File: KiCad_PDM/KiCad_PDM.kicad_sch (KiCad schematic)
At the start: 0 parts

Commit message: initial commit
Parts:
- added C1, C2: 1uF, symbol Device:C
- added C3: 2.2nF, symbol Device:C
- added C4: 10nF, symbol Device:C
- added D1, D4: MMSZ47202T1G, Diode_SMD:D_SOD-123, symbol PDM:onsemi MMSZ4702T1G
- added D2, D3: FR107, Diode_SMD:D_SOD-123, symbol PDM:JSMSEMI FR107
- added J1: 6437288-1, 6437288-1, symbol 6437288-1:6437288-1
- added R1: 39K, symbol Device:R
- added R2: 1K, symbol Device:R
- added R3: 5.1K, symbol Device:R
- added R4: 50, symbol Device:R
- added U1: NSG2000, Package_SO:SOP-8_3.76x4.96mm_P1.27mm, symbol PDM:NSG2000
- added U2: 2N7002, Package_TO_SOT_SMD:SOT-23_Handsoldering, symbol PDM:Nexperia 2N7002BK,215
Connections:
- new net: D4.1, R3.2, R4.1
- new net: C4.1, R4.2
- new net: C3.1, R1.2, R2.1, U1.3 (Osc)
- new net: R2.2, U2.3
- new net: C2.1, D1.1, D2.1, U1.8 (BST)
- new net: C2.2, D1.2, D3.2, U1.6 (TS)
- new net: R3.1, U2.1
- new net: D2.2, D3.1
- new net +BATT: C1.1, R1.1, U1.1 (VCC)
- new net Ch1: U1.2 (In)
- new net GND: C1.2, C3.2, D4.2, U1.4 (GND), U2.2

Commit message: initial commit
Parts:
- removed C1, C2: 1uF, symbol Device:C
- removed C3: 2.2nF, symbol Device:C
- removed C4: 10nF, symbol Device:C
- removed D1, D4: MMSZ47202T1G, Diode_SMD:D_SOD-123, symbol PDM:onsemi MMSZ4702T1G
- removed D2, D3: FR107, Diode_SMD:D_SOD-123, symbol PDM:JSMSEMI FR107
- removed R1: 39K, symbol Device:R
- removed R2: 1K, symbol Device:R
- removed R3: 5.1K, symbol Device:R
- removed R4: 50, symbol Device:R
- removed U1: NSG2000, Package_SO:SOP-8_3.76x4.96mm_P1.27mm, symbol PDM:NSG2000
- removed U2: 2N7002, Package_TO_SOT_SMD:SOT-23_Handsoldering, symbol PDM:Nexperia 2N7002BK,215
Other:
- added sheet Gate Driver (Gate Driver.kicad_sch)
- moved on the sheet: J1

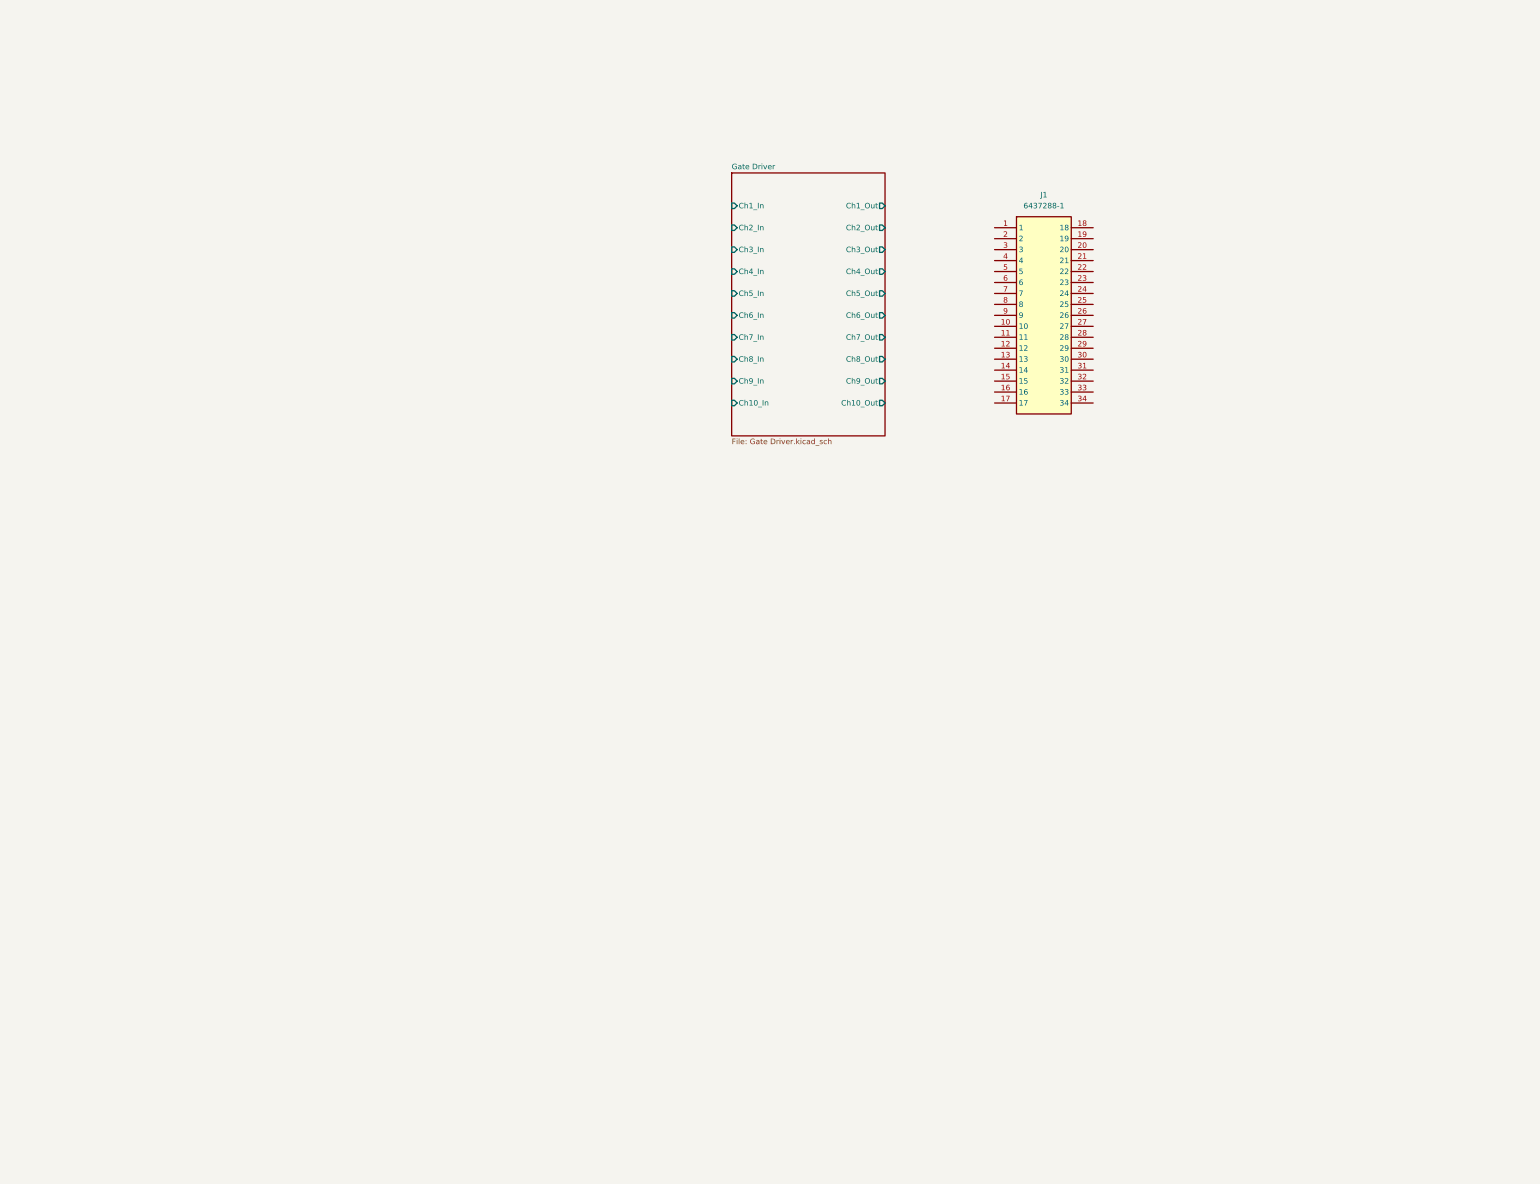
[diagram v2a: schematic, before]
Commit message: layout and tracing
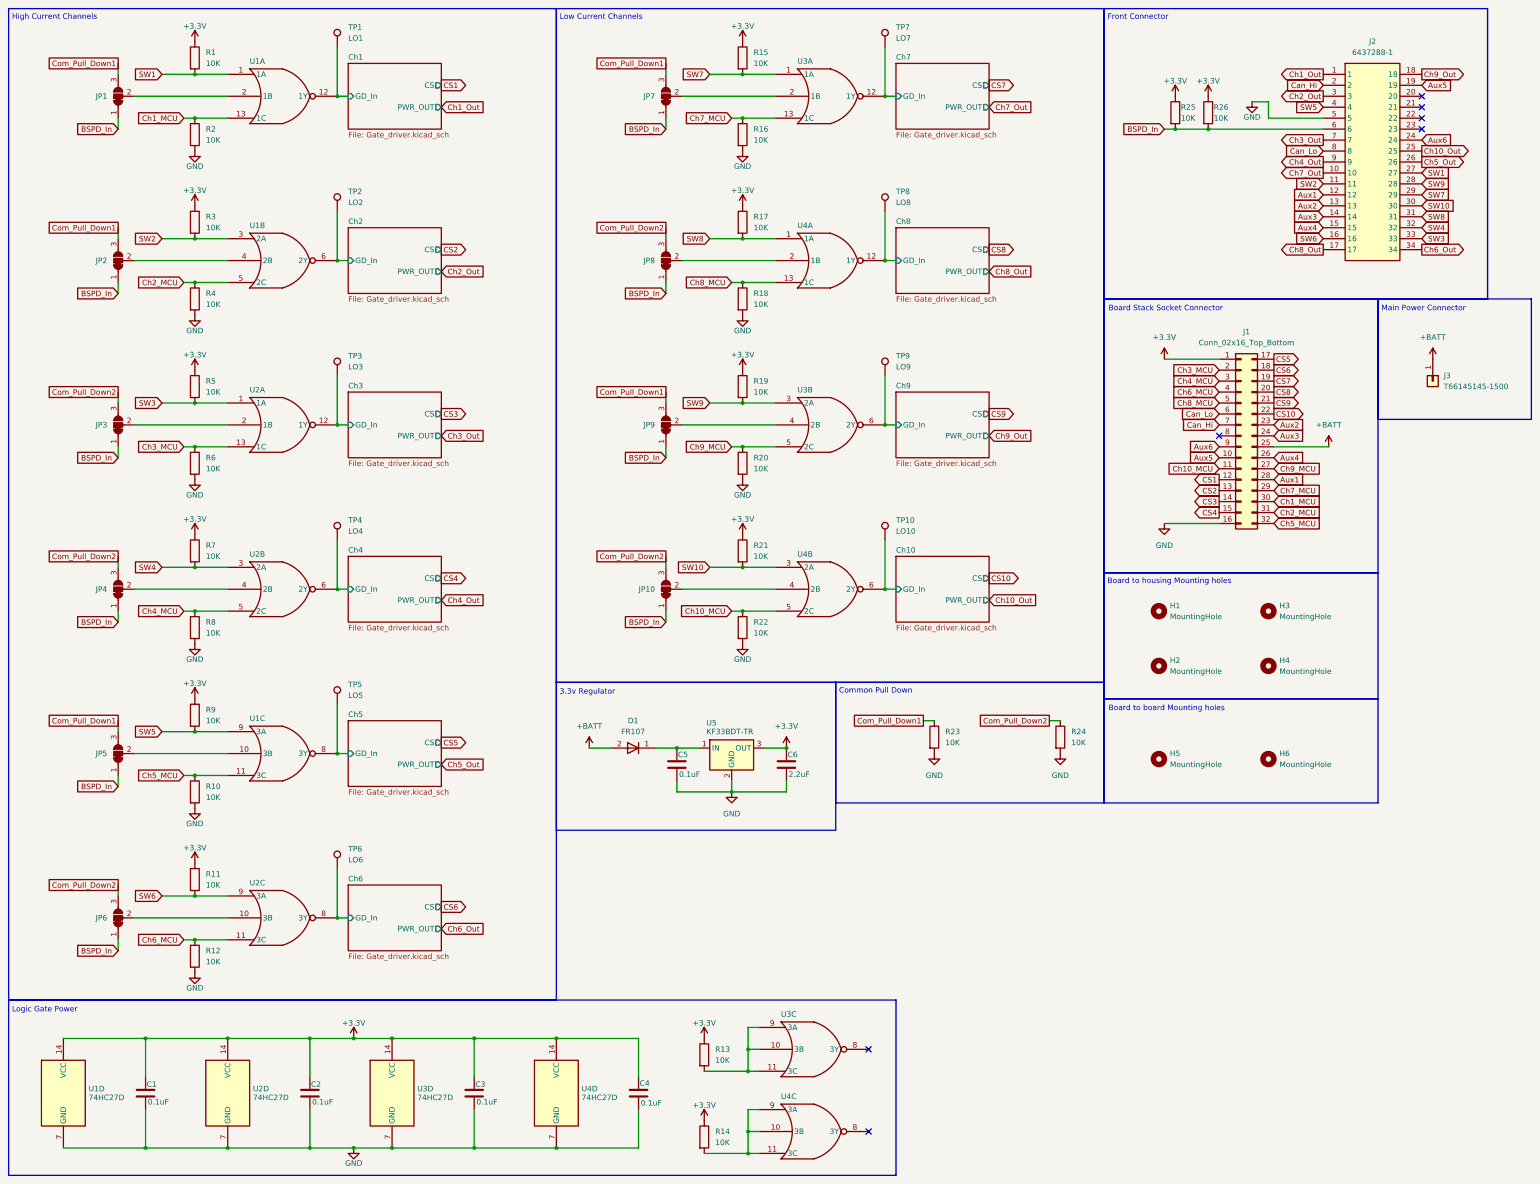
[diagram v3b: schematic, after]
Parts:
- added C1, C2, C3, C4, C5: 0.1uF, Capacitor_SMD:C_0805_2012Metric_Pad1.18x1.45mm_HandSolder, symbol Device:C
- added C6: 2.2uF, Capacitor_SMD:C_0805_2012Metric_Pad1.18x1.45mm_HandSolder, symbol Device:C
- added D1: FR107, Diode_SMD:D_SOD-123, symbol PDM:JSMSEMI FR107
- added H1, H2, H3, H4, H5, H6: MountingHole, MountingHolesCustom:MountingHole_NPTH_3.5_6.25SB, symbol Mechanical:MountingHole
- added J1: Conn_02x16_Top_Bottom, Connector_PinSocket_2.54mm:PinSocket_2x16_P2.54mm_Vertical, symbol Connector_Generic:Conn_02x16_Top_Bottom
- added J3: T66145145-1500, Custom_connector:XFCN T66145145-1500, symbol Connector_Generic:Conn_01x01
- added JP1, JP10, JP2, JP3, JP4, JP5, JP6, JP7, JP8, JP9: SolderJumper_3_Bridged12, Jumper:SolderJumper-3_P1.3mm_Bridged2Bar12_RoundedPad1.0x1.5mm_NumberLabels, symbol Jumper:SolderJumper_3_Bridged12
- added R1, R10, R11, R12, R13, R14, R15, R16, R17, R18, R19, R2, R20, R21, R22, R23, R24, R25, R26, R3, R4, R5, R6, R7, R8, R9: 10K, Resistor_SMD:R_0805_2012Metric_Pad1.20x1.40mm_HandSolder, symbol Device:R
- added TP1: LO1, Test Hook:Custom_Testpad, symbol Connector:TestPoint
- added TP10: LO10, Test Hook:Custom_Testpad, symbol Connector:TestPoint
- added TP2: LO2, Test Hook:Custom_Testpad, symbol Connector:TestPoint
- added TP3: LO3, Test Hook:Custom_Testpad, symbol Connector:TestPoint
- added TP4: LO4, Test Hook:Custom_Testpad, symbol Connector:TestPoint
- added TP5: LO5, Test Hook:Custom_Testpad, symbol Connector:TestPoint
- added TP6: LO6, Test Hook:Custom_Testpad, symbol Connector:TestPoint
- added TP7: LO7, Test Hook:Custom_Testpad, symbol Connector:TestPoint
- added TP8: LO8, Test Hook:Custom_Testpad, symbol Connector:TestPoint
- added TP9: LO9, Test Hook:Custom_Testpad, symbol Connector:TestPoint
- added U1, U2, U3, U4: 74HC27D, Package_SO:SOIC-14_3.9x8.7mm_P1.27mm, symbol Logic_gates:Nexperia_74HC27D
- added U5: KF33BDT-TR, Package_TO_SOT_SMD:TO-252-2, symbol LDO:ST KF33BDT-TR
- J2: renamed from J1; footprint 6437288-1 -> Custom_connector:6437288-1
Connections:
- net Ch1_Out: now reaches J2.1
- net Ch7_Out: now reaches J2.10
- net SW2: now reaches J2.11
- net SW2: now also R3.2, U1.3 (2A)
- net Aux1: now reaches J2.12
- net Aux1: now also J1.28 (Pin_28)
- net Aux2: now reaches J2.13
- net Aux2: now also J1.23 (Pin_23)
- net Aux3: now reaches J2.14
- net Aux3: now also J1.24 (Pin_24)
- net Aux4: now reaches J2.15
- net Aux4: now also J1.26 (Pin_26)
- net SW6: now reaches J2.16
- net SW6: now also R11.2, U2.9 (3A)
- net Ch8_Out: now reaches J2.17
- net Ch9_Out: now reaches J2.18
- net Aux5: now reaches J2.19
- net Aux5: now also J1.10 (Pin_10)
- net Can_Hi: now reaches J2.2
- net Can_Hi: now also J1.7 (Pin_7)
- net Aux6: now reaches J2.24
- net Aux6: now also J1.9 (Pin_9)
- net Ch10_Out: now reaches J2.25
- net Ch5_Out: now reaches J2.26
- net SW1: now reaches J2.27
- net SW1: now also R1.2, U1.1 (1A)
- net SW9: now reaches J2.28
- net SW9: now also R19.2, U3.3 (2A)
- net SW7: now reaches J2.29
- net SW7: now also R15.2, U3.1 (1A)
- net Ch2_Out: now reaches J2.3
- net SW10: now reaches J2.30
- net SW10: now also R21.2, U4.3 (2A)
- net SW8: now reaches J2.31
- net SW8: now also R17.2, U4.1 (1A)
- net SW4: now reaches J2.32
- net SW4: now also R7.2, U2.3 (2A)
- net SW3: now reaches J2.33
- net SW3: now also R5.2, U2.1 (1A)
- net Ch6_Out: now reaches J2.34
- net SW5: now reaches J2.4
- net SW5: now also R9.2, U1.9 (3A)
- net GND: now reaches J2.5
- net GND: now also C1.2, C2.2, C3.2, C4.2, C5.2, C6.2, J1.16 (Pin_16), R10.2, R12.2, R16.2, R18.2, R2.2, R20.2, R22.2, R23.2, R24.2, R4.2, R6.2, R8.2, U1.7 (GND), U2.7 (GND), U3.7 (GND), U4.7 (GND), U5.2 (GND)
- net BSPD_In: now reaches J2.6
- net BSPD_In: now also JP1.1 (A), JP10.1 (A), JP2.1 (A), JP3.1 (A), JP4.1 (A), JP5.1 (A), JP6.1 (A), JP7.1 (A), JP8.1 (A), JP9.1 (A), R25.2, R26.2
- net Ch3_Out: now reaches J2.7
- net Can_Lo: now reaches J2.8
- net Can_Lo: now also J1.6 (Pin_6)
- net Ch4_Out: now reaches J2.9
- new net: C5.1, D1.1, U5.1 (IN)
- new net: JP8.2 (C), U4.2 (1B)
- new net: JP9.2 (C), U3.4 (2B)
- new net: R13.2, U3.10 (3B), U3.11 (3C), U3.9 (3A)
- new net: JP4.2 (C), U2.4 (2B)
- new net: JP10.2 (C), U4.4 (2B)
- new net: JP7.2 (C), U3.2 (1B)
- new net: R14.2, U4.10 (3B), U4.11 (3C), U4.9 (3A)
- new net: JP3.2 (C), U2.2 (1B)
- new net: JP5.2 (C), U1.10 (3B)
- new net: JP2.2 (C), U1.4 (2B)
- new net: JP1.2 (C), U1.2 (1B)
- new net: JP6.2 (C), U2.10 (3B)
- new net +3.3V: C1.1, C2.1, C3.1, C4.1, C6.1, J1.1 (Pin_1), R1.1, R11.1, R13.1, R14.1, R15.1, R17.1, R19.1, R21.1, R25.1, R26.1, R3.1, R5.1, R7.1, R9.1, U1.14 (VCC), U2.14 (VCC), U3.14 (VCC), U4.14 (VCC), U5.3 (OUT)
- new net +BATT: D1.2, J1.25 (Pin_25), J3.1 (Pin_1)
- new net CS1: J1.12 (Pin_12)
- new net CS10: J1.22 (Pin_22)
- new net CS2: J1.13 (Pin_13)
- new net CS3: J1.14 (Pin_14)
- new net CS4: J1.15 (Pin_15)
- new net CS5: J1.17 (Pin_17)
- new net CS6: J1.18 (Pin_18)
- new net CS7: J1.19 (Pin_19)
- new net CS8: J1.20 (Pin_20)
- new net CS9: J1.21 (Pin_21)
- new net Ch1/GD_In: TP1.1, U1.12 (1Y)
- new net Ch10/GD_In: TP10.1, U4.6 (2Y)
- new net Ch10_MCU: J1.11 (Pin_11), R22.1, U4.5 (2C)
- new net Ch1_MCU: J1.30 (Pin_30), R2.1, U1.13 (1C)
- new net Ch2/GD_In: TP2.1, U1.6 (2Y)
- new net Ch2_MCU: J1.31 (Pin_31), R4.1, U1.5 (2C)
- new net Ch3/GD_In: TP3.1, U2.12 (1Y)
- new net Ch3_MCU: J1.2 (Pin_2), R6.1, U2.13 (1C)
- new net Ch4/GD_In: TP4.1, U2.6 (2Y)
- new net Ch4_MCU: J1.3 (Pin_3), R8.1, U2.5 (2C)
- new net Ch5/GD_In: TP5.1, U1.8 (3Y)
- new net Ch5_MCU: J1.32 (Pin_32), R10.1, U1.11 (3C)
- new net Ch6/GD_In: TP6.1, U2.8 (3Y)
- new net Ch6_MCU: J1.4 (Pin_4), R12.1, U2.11 (3C)
- new net Ch7/GD_In: TP7.1, U3.12 (1Y)
- new net Ch7_MCU: J1.29 (Pin_29), R16.1, U3.13 (1C)
- new net Ch8/GD_In: TP8.1, U4.12 (1Y)
- new net Ch8_MCU: J1.5 (Pin_5), R18.1, U4.13 (1C)
- new net Ch9/GD_In: TP9.1, U3.6 (2Y)
- new net Ch9_MCU: J1.27 (Pin_27), R20.1, U3.5 (2C)
- new net Com_Pull_Down1: JP1.3 (B), JP2.3 (B), JP5.3 (B), JP7.3 (B), JP9.3 (B), R23.1
- new net Com_Pull_Down2: JP10.3 (B), JP3.3 (B), JP4.3 (B), JP6.3 (B), JP8.3 (B), R24.1
- no-connect marks 0 -> 7
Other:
- sheet Gate Driver renamed Ch1
- added sheet Ch10 (Gate_driver.kicad_sch)
- added sheet Ch2 (Gate_driver.kicad_sch)
- added sheet Ch3 (Gate_driver.kicad_sch)
- added sheet Ch4 (Gate_driver.kicad_sch)
- added sheet Ch5 (Gate_driver.kicad_sch)
- added sheet Ch6 (Gate_driver.kicad_sch)
- added sheet Ch7 (Gate_driver.kicad_sch)
- added sheet Ch8 (Gate_driver.kicad_sch)
- added sheet Ch9 (Gate_driver.kicad_sch)
- sheet Ch1: file Gate Driver.kicad_sch -> Gate_driver.kicad_sch
- sheet Ch1 ports: added CS, GD_In, PWR_OUT; removed Ch10_In, Ch10_Out, Ch1_In, Ch1_Out, Ch2_In, Ch2_Out, Ch3_In, Ch3_Out, Ch4_In, Ch4_Out, Ch5_In, Ch5_Out, Ch6_In, Ch6_Out, Ch7_In, Ch7_Out, Ch8_In, Ch8_Out, Ch9_In, Ch9_Out
- note added: "3.3v Regulator"
- note added: "Board Stack Socket Connector"
- note added: "Board to board Mounting holes"
- note added: "Board to housing Mounting holes"
- note added: "Common Pull Down"
- note added: "Front Connector"
- note added: "High Current Channels"
- note added: "Logic Gate Power"
- note added: "Low Current Channels"
- note added: "Main Power Connector"
- moved on the sheet: J2

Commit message: MK1
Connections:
- net +3.3V: now also J1.4 (Pin_4); no longer J1.1 (Pin_1)
- net +BATT: now also J1.17 (Pin_17); no longer J1.25 (Pin_25)
- net Aux1: now also J1.19 (Pin_19), J2.4; no longer J1.28 (Pin_28), J2.12
- net Aux2: now also J1.20 (Pin_20); no longer J1.23 (Pin_23)
- net Aux3: now also J1.18 (Pin_18); no longer J1.24 (Pin_24)
- net Aux4: now also J1.16 (Pin_16); no longer J1.26 (Pin_26)
- net Aux5: now also J1.21 (Pin_21), J2.12; no longer J1.10 (Pin_10), J2.19
- net Aux6: now also J1.15 (Pin_15), J2.6; no longer J1.9 (Pin_9), J2.24
- net BSPD_In: now also J2.21; no longer J2.6
- net CS1: now also J1.31 (Pin_31); no longer J1.12 (Pin_12)
- net CS10: now also J1.7 (Pin_7); no longer J1.22 (Pin_22)
- net CS2: now also J1.22 (Pin_22); no longer J1.13 (Pin_13)
- net CS3: now also J1.11 (Pin_11); no longer J1.14 (Pin_14)
- net CS4: now also J1.3 (Pin_3); no longer J1.15 (Pin_15)
- net CS5: now also J1.24 (Pin_24); no longer J1.17 (Pin_17)
- net CS6: now also J1.9 (Pin_9); no longer J1.18 (Pin_18)
- net CS7: now also J1.27 (Pin_27); no longer J1.19 (Pin_19)
- net CS8: now also J1.2 (Pin_2); no longer J1.20 (Pin_20)
- net CS9: now also J1.25 (Pin_25); no longer J1.21 (Pin_21)
- net Can_Hi: now also J1.23 (Pin_23), J2.11; no longer J1.7 (Pin_7), J2.2
- net Can_Lo: now also J1.13 (Pin_13); no longer J1.6 (Pin_6)
- net Ch10_MCU: now also J1.5 (Pin_5); no longer J1.11 (Pin_11)
- net Ch1_MCU: now also J1.26 (Pin_26); no longer J1.30 (Pin_30)
- net Ch2_MCU: now also J1.30 (Pin_30); no longer J1.31 (Pin_31)
- net Ch3_MCU: now also J1.6 (Pin_6); no longer J1.2 (Pin_2)
- net Ch4_MCU: now also J1.10 (Pin_10); no longer J1.3 (Pin_3)
- net Ch5_MCU: now also J1.28 (Pin_28); no longer J1.32 (Pin_32)
- net Ch6_MCU: now also J1.8 (Pin_8); no longer J1.4 (Pin_4)
- net Ch7_MCU: now also J1.32 (Pin_32); no longer J1.29 (Pin_29)
- net Ch8_MCU: now also J1.1 (Pin_1); no longer J1.5 (Pin_5)
- net Ch9_MCU: now also J1.29 (Pin_29); no longer J1.27 (Pin_27)
- net GND: now also J1.14 (Pin_14); no longer J1.16 (Pin_16)
- net SW1: now also J2.19; no longer J2.27
- net SW2: now also J2.27; no longer J2.11
- net SW5: now also J2.2; no longer J2.4
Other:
- moved on the sheet: R25, R26

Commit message: updated design and 3d models
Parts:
- renumbered H5 to H3, H3 to H4, H4 to H5, R26 to R25, R25 to R26
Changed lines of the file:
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@@
 		(dnp no)
 		(fields_autoplaced yes)
-		(property "Reference" "#PWR036"
+		(property "Reference" "#PWR034"
 			(at 342.9 97.79 0)
 			(effects
@@
 			(project "KiCad_PDM"
 				(path "/d452ee35-fb49-4a7c-9bf6-fa2f0e97aadb"
-					(reference "#PWR036")
+					(reference "#PWR034")
 					(unit 1)
 				)
@@
 		(dnp no)
 		(fields_autoplaced yes)
-		(property "Reference" "#PWR035"
+		(property "Reference" "#PWR033"
 			(at 318.77 97.79 0)
 			(effects
@@
 			(project "KiCad_PDM"
 				(path "/d452ee35-fb49-4a7c-9bf6-fa2f0e97aadb"
-					(reference "#PWR035")
+					(reference "#PWR033")
 					(unit 1)
 				)
@@
 		(on_board yes)
 		(dnp no)
-		(property "Reference" "#PWR034"
+		(property "Reference" "#PWR032"
 			(at 300.99 40.64 0)
 			(effects
@@
 			(project "KiCad_PDM"
 				(path "/d452ee35-fb49-4a7c-9bf6-fa2f0e97aadb"
-					(reference "#PWR034")
+					(reference "#PWR032")
 					(unit 1)
 				)
@@
 		(dnp no)
 		(fields_autoplaced yes)
-		(property "Reference" "H3"
+		(property "Reference" "H4"
 			(at 307.34 151.1299 0)
 			(effects
@@
 			(project "KiCad_PDM"
 				(path "/d452ee35-fb49-4a7c-9bf6-fa2f0e97aadb"
-					(reference "H3")
+					(reference "H4")
 					(unit 1)
 				)
@@
 		(on_board yes)
 		(dnp no)
-		(property "Reference" "#PWR033"
+		(property "Reference" "#PWR035"
 			(at 367.03 31.75 0)
 			(effects
@@
 			(project "KiCad_PDM"
 				(path "/d452ee35-fb49-4a7c-9bf6-fa2f0e97aadb"
-					(reference "#PWR033")
+					(reference "#PWR035")
 					(unit 1)
 				)
@@
 		(dnp no)
 		(fields_autoplaced yes)
-		(property "Reference" "H4"
+		(property "Reference" "H5"
 			(at 307.34 163.8299 0)
 			(effects
@@
 			(project "KiCad_PDM"
 				(path "/d452ee35-fb49-4a7c-9bf6-fa2f0e97aadb"
-					(reference "H4")
+					(reference "H5")
 					(unit 1)
 				)
@@
 		(on_board yes)
 		(dnp no)
-		(property "Reference" "R26"
+		(property "Reference" "R25"
 			(at 365.76 30.48 0)
 			(effects
@@
 			(project "KiCad_PDM"
 				(path "/d452ee35-fb49-4a7c-9bf6-fa2f0e97aadb"
-					(reference "R26")
+					(reference "R25")
 					(unit 1)
 				)
@@
 			)
 		)
-		(property "Datasheet" "~"
+		(property "Datasheet" "https://www.lcsc.com/product-detail/C7499351.html"
 			(at 298.45 111.76 0)
 			(effects
@@
 		(on_board yes)
 		(dnp no)
-		(property "Reference" "R25"
+		(property "Reference" "R26"
 			(at 373.38 30.48 0)
 			(effects
@@
 			(project "KiCad_PDM"
 				(path "/d452ee35-fb49-4a7c-9bf6-fa2f0e97aadb"
-					(reference "R25")
+					(reference "R26")
 					(unit 1)
 				)
@@
 		(on_board yes)
 		(dnp no)
-		(property "Reference" "#PWR032"
+		(property "Reference" "#PWR036"
 			(at 374.65 31.75 0)
 			(effects
@@
 			(project "KiCad_PDM"
 				(path "/d452ee35-fb49-4a7c-9bf6-fa2f0e97aadb"
-					(reference "#PWR032")
+					(reference "#PWR036")
 					(unit 1)
 				)
@@
 		(dnp no)
 		(fields_autoplaced yes)
-		(property "Reference" "H5"
+		(property "Reference" "H3"
 			(at 281.94 185.4199 0)
 			(effects
@@
 			(project "KiCad_PDM"
 				(path "/d452ee35-fb49-4a7c-9bf6-fa2f0e97aadb"
-					(reference "H5")
+					(reference "H3")
 					(unit 1)
 				)
